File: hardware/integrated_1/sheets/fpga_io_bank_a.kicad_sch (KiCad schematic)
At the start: 10 parts, among them J4 Conn_01x12, U1 XC6SLX9-TQG144, U8 XLH335200.000000I

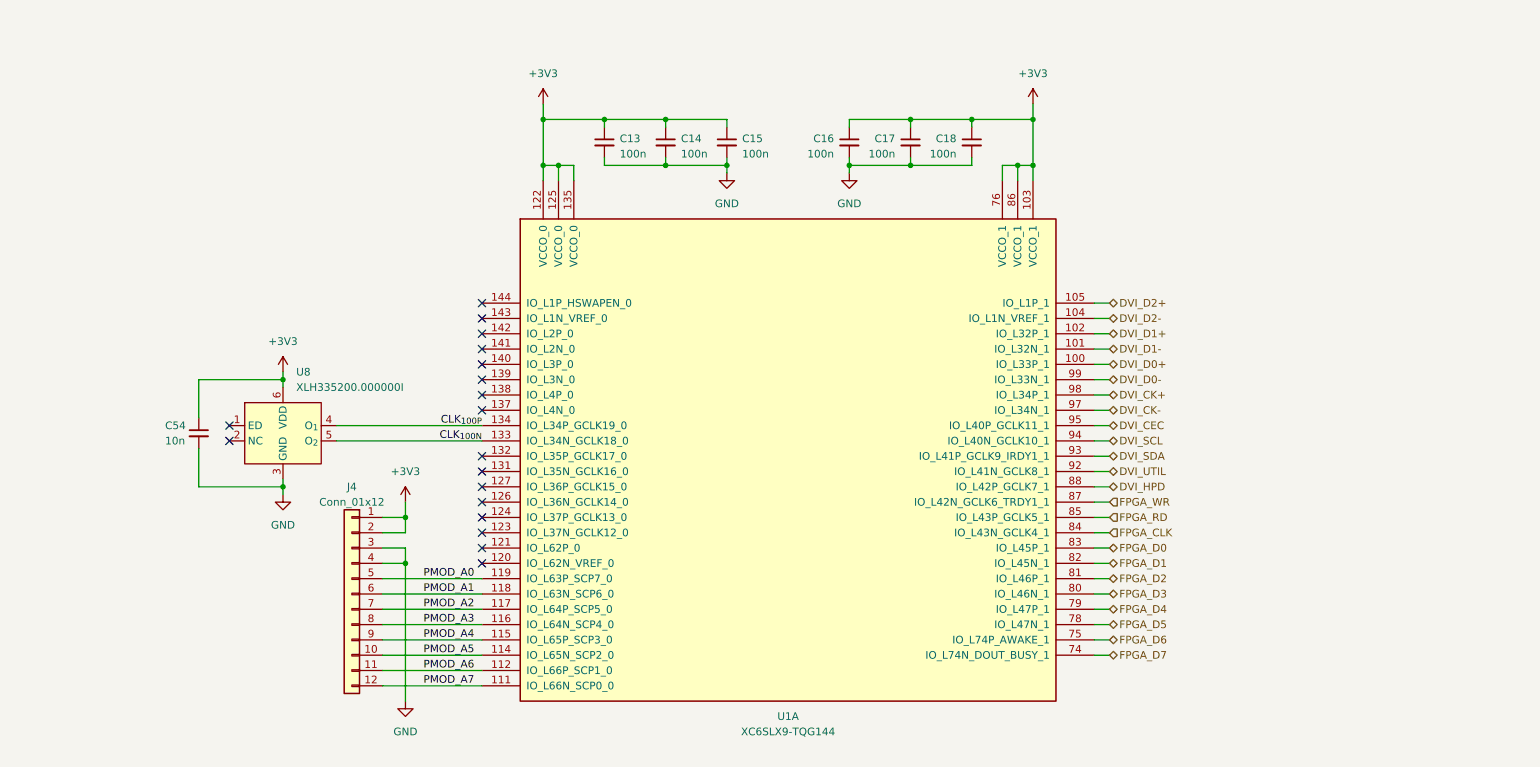
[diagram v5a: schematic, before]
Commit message: added testpoints
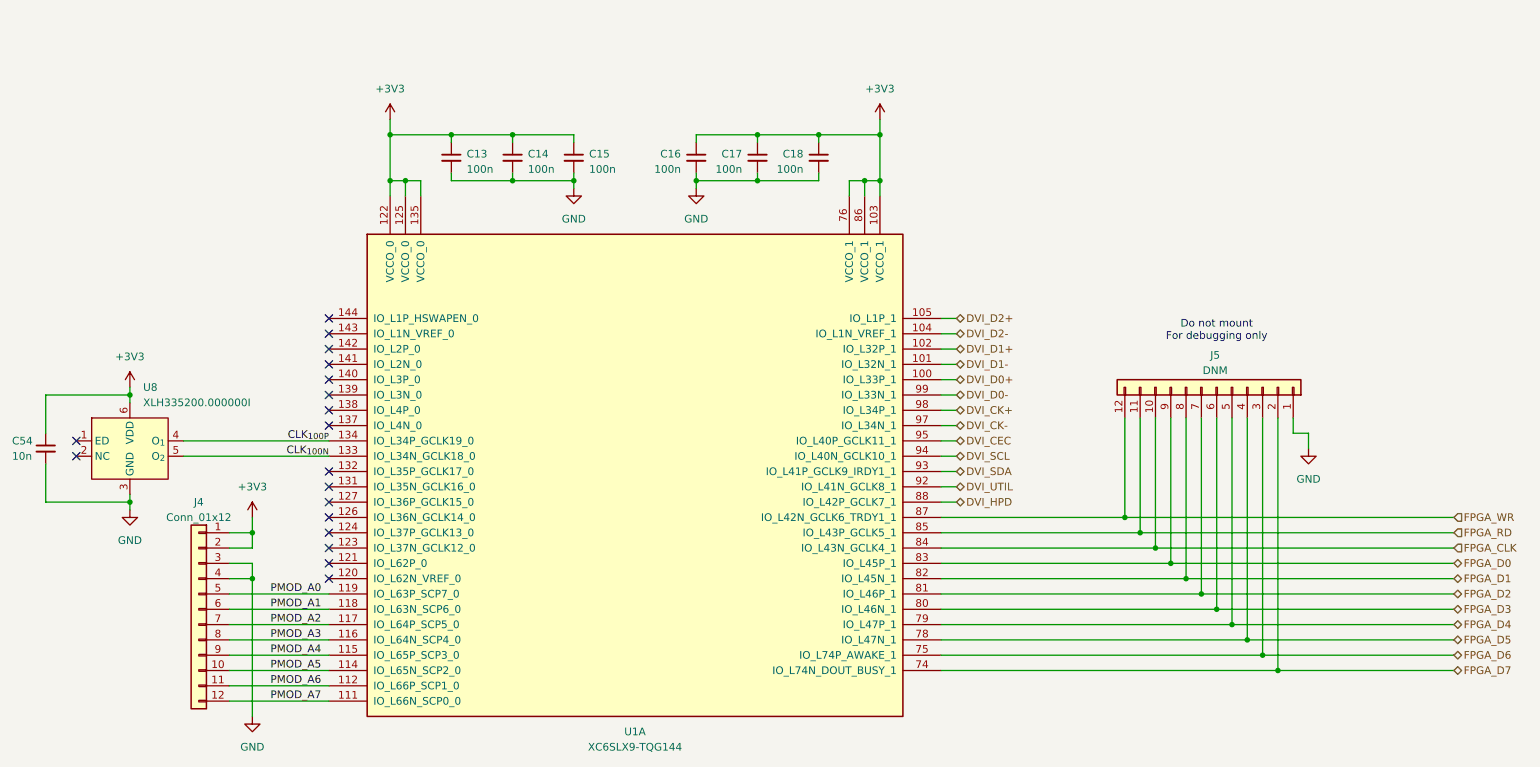
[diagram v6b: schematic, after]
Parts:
- added J5: DNM, Connector_PinHeader_1.00mm:PinHeader_2x06_P1.00mm_Vertical_SMD, symbol Connector_Generic:Conn_01x12
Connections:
- net FPGA_CLK: now also J5.10 (Pin_10)
- net FPGA_D0: now also J5.9 (Pin_9)
- net FPGA_D1: now also J5.8 (Pin_8)
- net FPGA_D2: now also J5.7 (Pin_7)
- net FPGA_D3: now also J5.6 (Pin_6)
- net FPGA_D4: now also J5.5 (Pin_5)
- net FPGA_D5: now also J5.4 (Pin_4)
- net FPGA_D6: now also J5.3 (Pin_3)
- net FPGA_D7: now also J5.2 (Pin_2)
- net FPGA_RD: now also J5.11 (Pin_11)
- net FPGA_WR: now also J5.12 (Pin_12)
- net GND: now also J5.1 (Pin_1)
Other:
- note added: "Do not mount For debugging only"
- moved on the sheet: C13, C14, C15, C16, C17, C18, C54, J4, U1A, U8
